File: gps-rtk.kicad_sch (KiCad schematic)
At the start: 24 parts, among them J400 Conn_Coaxial, U401 ZED-F9P

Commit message: [RF gps] update rev 1.1 fixed  update  rf place
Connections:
- net RF_: now reaches C419.2, L400.2, R415.1
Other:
- moved on the sheet: R415
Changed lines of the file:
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@@
 	(wire
 		(pts
-			(xy 227.33 74.93) (xy 228.6 74.93)
+			(xy 227.33 74.93) (xy 237.49 74.93)
 		)
 		(stroke
@@
 	(wire
 		(pts
-			(xy 236.22 74.93) (xy 243.84 74.93)
+			(xy 245.11 74.93) (xy 252.73 74.93)
 		)
 		(stroke
@@
 	)
 	(label "VCC_RF"
-		(at 243.84 74.93 180)
+		(at 252.73 74.93 180)
 		(effects
 			(font
@@
 	(label "GPS_EXINTERUPT"
 		(at 58.42 187.96 180)
+		(effects
+			(font
+				(size 1.27 1.27)
+			)
+			(justify right bottom)
+		)
+	)
+	(label "RF_"
+		(at 233.68 74.93 180)
 		(effects
 			(font
@@
 	(symbol
 		(lib_id "PCM_JLCPCB-Resistors:0402,10Ω")
-		(at 232.41 74.93 90)
+		(at 241.3 74.93 90)
 		(unit 1)
 		(exclude_from_sim no)
@@
 		(dnp no)
 		(property "Reference" "R415"
-			(at 232.4099 72.39 0)
+			(at 241.2999 72.39 0)
 			(effects
 				(font
@@
 		)
 		(property "Value" "10Ω"
-			(at 232.41 74.93 90)
+			(at 241.3 74.93 90)
 			(do_not_autoplace yes)
 			(effects
@@
 		)
 		(property "Footprint" "PCM_JLCPCB:R_0402"
-			(at 232.41 76.708 90)
+			(at 241.3 76.708 90)
 			(effects
 				(font
@@
 		)
 		(property "Datasheet" "https://www.lcsc.com/datasheet/lcsc_datasheet_2205311900_UNI-ROYAL-Uniroyal-Elec-0402WGF100JTCE_C25077.pdf"
-			(at 232.41 74.93 0)
+			(at 241.3 74.93 0)
 			(effects
 				(font
@@
 		)
 		(property "Description" "62.5mW Thick Film Resistors 50V ±1% ±200ppm/°C 10Ω 0402 Chip Resistor - Surface Mount ROHS"
-			(at 232.41 74.93 0)
+			(at 241.3 74.93 0)
 			(effects
 				(font
@@
 		)
 		(property "LCSC" "C25077"
-			(at 232.41 74.93 0)
+			(at 241.3 74.93 0)
 			(effects
 				(font
@@
 		)
 		(property "Stock" "2241750"
-			(at 232.41 74.93 0)
+			(at 241.3 74.93 0)
 			(effects
 				(font
@@
 		)
 		(property "Price" "0.004USD"
-			(at 232.41 74.93 0)
+			(at 241.3 74.93 0)
 			(effects
 				(font
@@
 		)
 		(property "Process" "SMT"
-			(at 232.41 74.93 0)
+			(at 241.3 74.93 0)
 			(effects
 				(font
@@
 		)
 		(property "Minimum Qty" "20"
-			(at 232.41 74.93 0)
+			(at 241.3 74.93 0)
 			(effects
 				(font
@@
 		)
 		(property "Attrition Qty" "10"
-			(at 232.41 74.93 0)
+			(at 241.3 74.93 0)
 			(effects
 				(font
@@
 		)
 		(property "Class" "Basic Component"
-			(at 232.41 74.93 0)
+			(at 241.3 74.93 0)
 			(effects
 				(font
@@
 		)
 		(property "Category" "Resistors,Chip Resistor - Surface Mount"
-			(at 232.41 74.93 0)
+			(at 241.3 74.93 0)
 			(effects
 				(font
@@
 		)
 		(property "Manufacturer" "UNI-ROYAL(Uniroyal Elec)"
-			(at 232.41 74.93 0)
+			(at 241.3 74.93 0)
 			(effects
 				(font
@@
 		)
 		(property "Part" "0402WGF100JTCE"
-			(at 232.41 74.93 0)
+			(at 241.3 74.93 0)
 			(effects
 				(font
@@
 		)
 		(property "Resistance" "10Ω"
-			(at 232.41 74.93 0)
+			(at 241.3 74.93 0)
 			(effects
 				(font
@@
 		)
 		(property "Power(Watts)" "62.5mW"
-			(at 232.41 74.93 0)
+			(at 241.3 74.93 0)
 			(effects
 				(font
@@
 		)
 		(property "Type" "Thick Film Resistors"
-			(at 232.41 74.93 0)
+			(at 241.3 74.93 0)
 			(effects
 				(font
@@
 		)
 		(property "Overload Voltage (Max)" "50V"
-			(at 232.41 74.93 0)
+			(at 241.3 74.93 0)
 			(effects
 				(font
@@
 		)
 		(property "Operating Temperature Range" "-55°C~+155°C"
-			(at 232.41 74.93 0)
+			(at 241.3 74.93 0)
 			(effects
 				(font
@@
 		)
 		(property "Tolerance" "±1%"
-			(at 232.41 74.93 0)
+			(at 241.3 74.93 0)
 			(effects
 				(font
@@
 		)
 		(property "Temperature Coefficient" "±200ppm/°C"
-			(at 232.41 74.93 0)
-			(effects
-				(font
+			(at 241.3 74.93 0)
+			(effects
+				(font

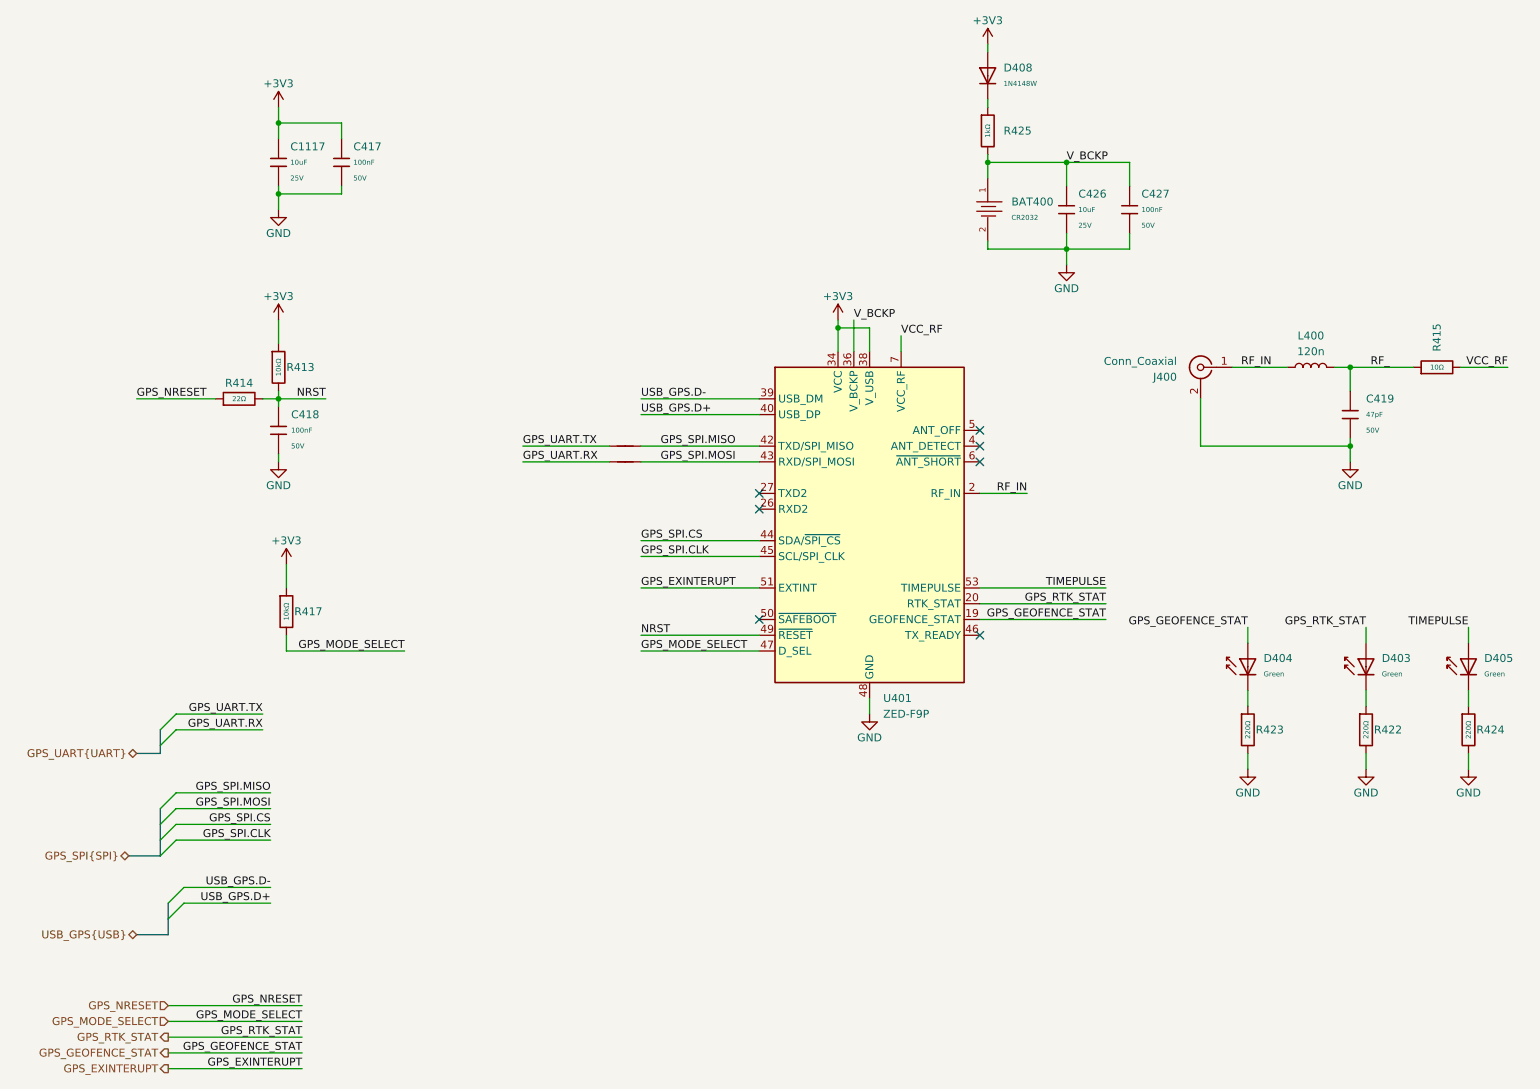
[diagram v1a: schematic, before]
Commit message: final check , added pull up resistors on i2c
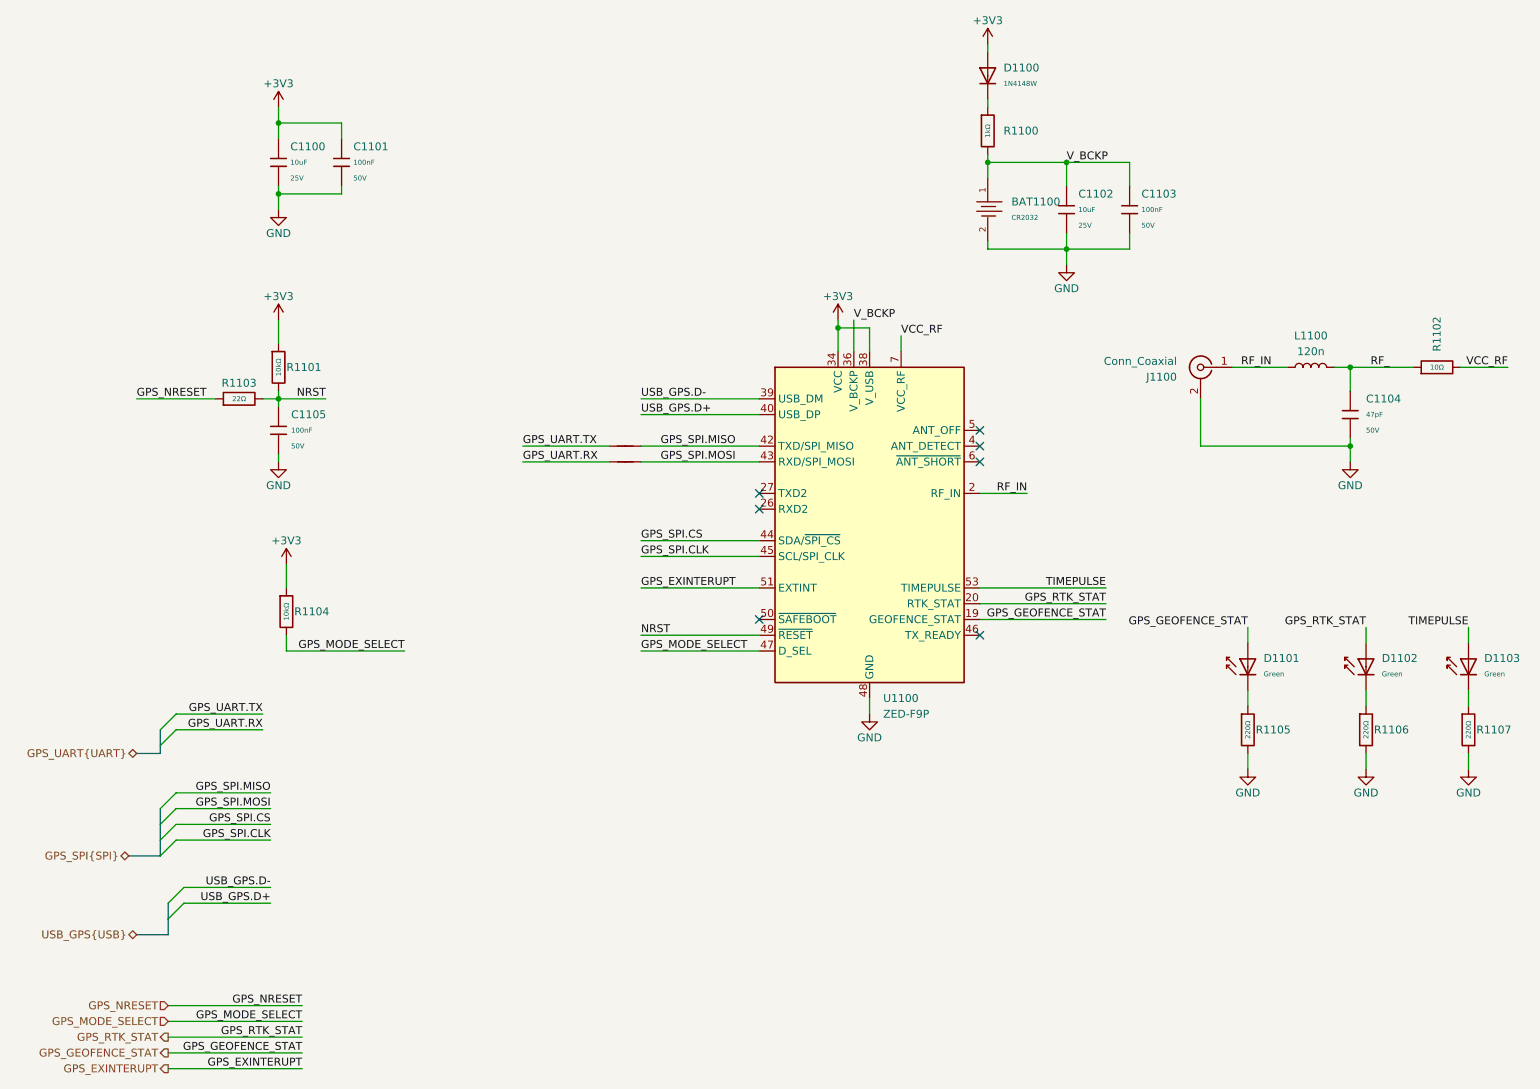
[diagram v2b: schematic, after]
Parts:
- renumbered BAT400 to BAT1100, C1117 to C1100, C417 to C1101, C426 to C1102, C427 to C1103, C419 to C1104, C418 to C1105, D408 to D1100, D404 to D1101, D403 to D1102, D405 to D1103, J400 to J1100, L400 to L1100, NT400 to NT1100, NT401 to NT1101, R425 to R1100, R413 to R1101, R415 to R1102, R414 to R1103, R417 to R1104, R423 to R1105, R422 to R1106, R424 to R1107, U401 to U1100
